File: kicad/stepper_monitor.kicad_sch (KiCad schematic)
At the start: 62 parts, among them J1 Conn_01x04_Pin, J2 Conn_01x04_Pin, J3 Conn_01x02_Pin, J4 USB_C_Receptacle_USB2.0, J5 JTAG, J6 Conn_01x04_Pin, M1 Motor-simple_stepper_motor_an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, Q1 MMDT2222A, SW1 SW_Push, U1 5V, U2 CP2102N-A01-GQFN28, U3 AMS1117-3.3, U4 CC6920BSO-5A, U5 CC6920BSO-5A, U6 ESP32-WROOM-32U-N4

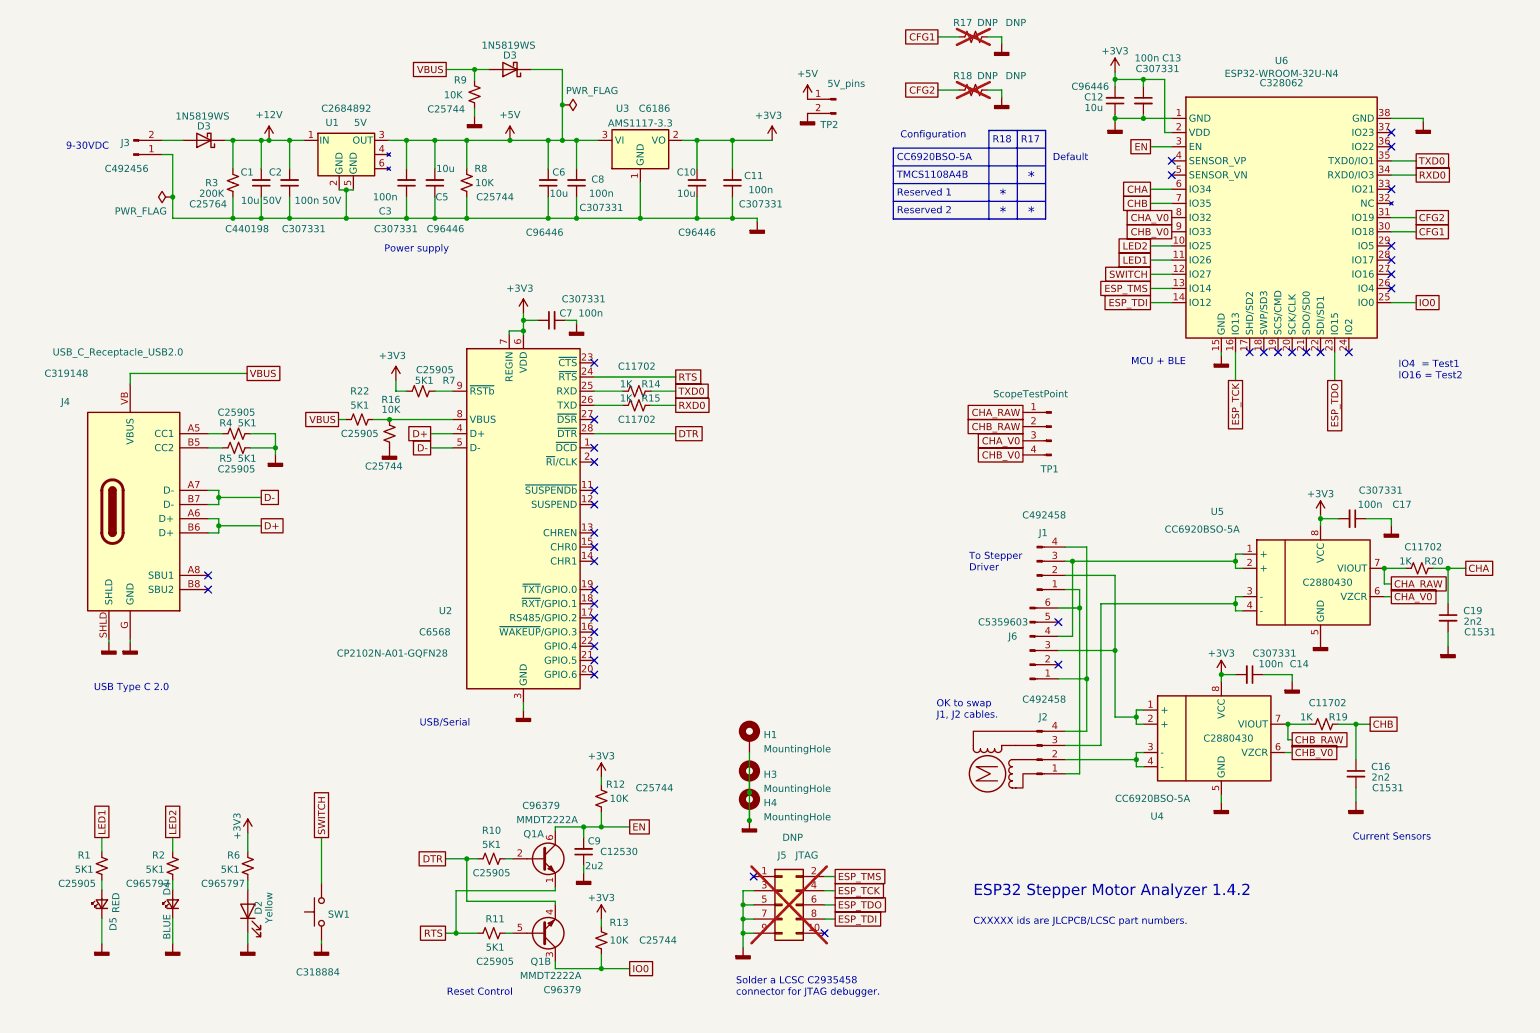
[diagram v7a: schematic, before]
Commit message: Routed opamp for voltage measurement. Added 4th mount hole
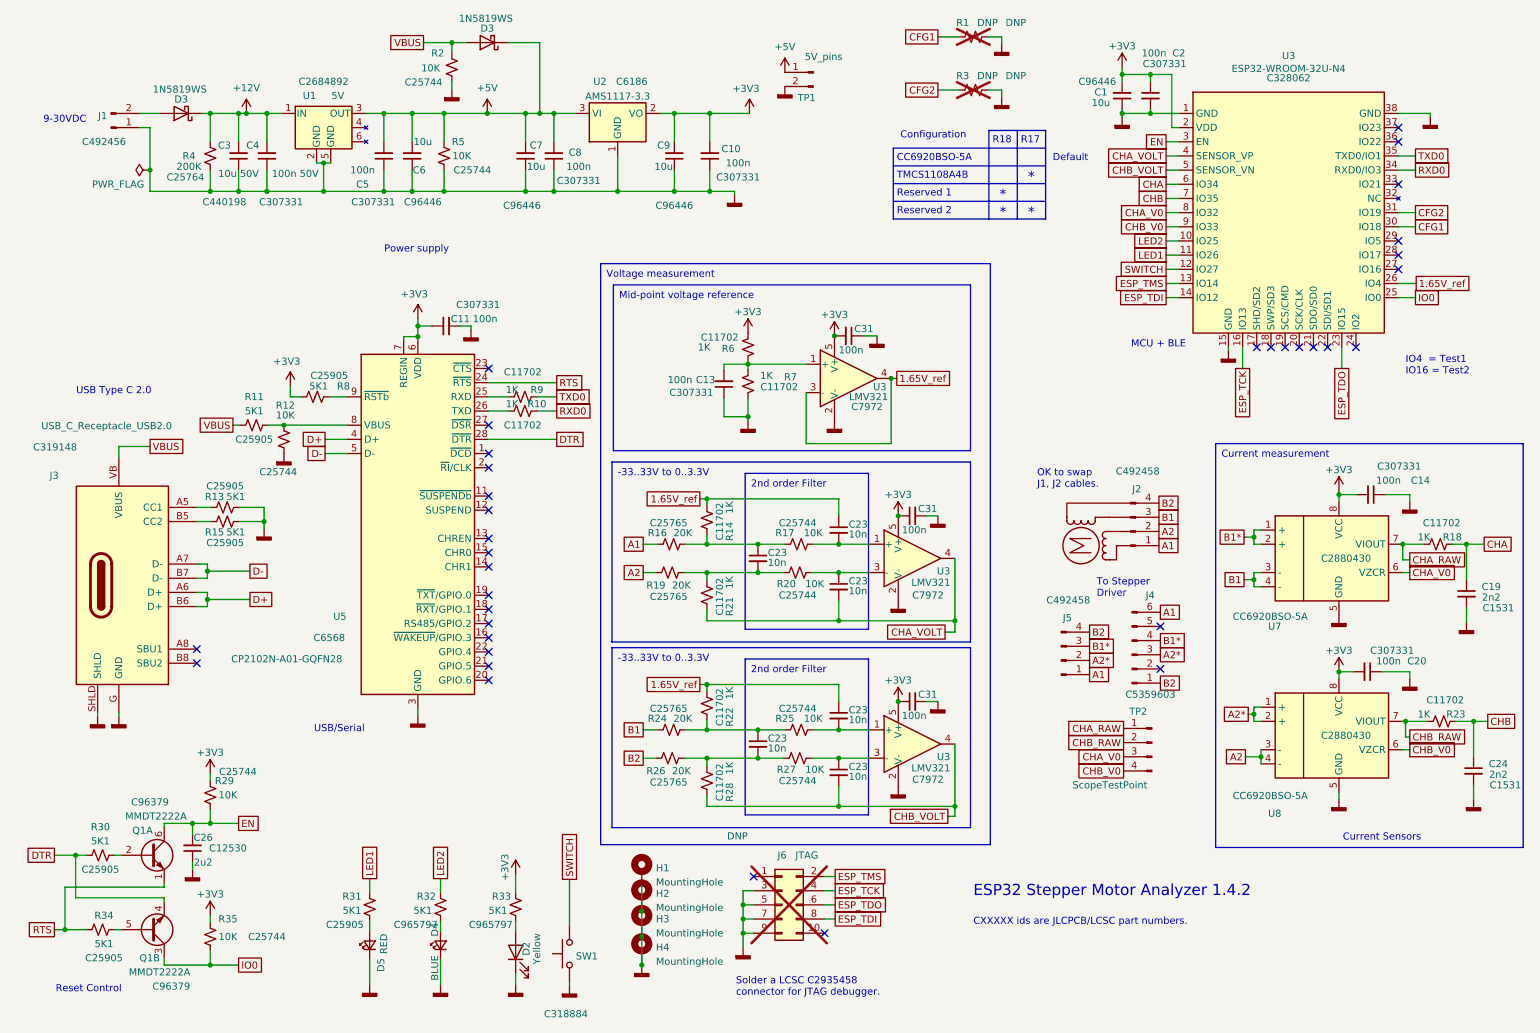
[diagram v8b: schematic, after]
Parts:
- added C13, C31 (x3): 100n, Capacitor_SMD:C_0402_1005Metric, symbol Device:C_Small
- added C23 (x6): 10n, Capacitor_SMD:C_0402_1005Metric, symbol Device:C_Small
- added H2: MountingHole, MountingHole:MountingHole_3.2mm_M3_Pad_Via, symbol Mechanical:MountingHole_Pad
- added R14, R21, R22, R28, R6, R7: 1K, Resistor_SMD:R_0402_1005Metric, symbol Device:R_Small_US
- added R16, R19, R24, R26: 20K, Resistor_SMD:R_0402_1005Metric, symbol Device:R_Small_US
- added R17, R20, R25, R27: 10K, Resistor_SMD:R_0402_1005Metric, symbol Device:R_Small_US
- added U3 (x3): LMV321, Package_TO_SOT_SMD:SOT-23-5, symbol Amplifier_Operational:LMV321
- renumbered C12 to C1, C11 to C10, C7 to C11, C17 to C14, C13 to C2, C14 to C20, C16 to C24, C9 to C26, C1 to C3, C2 to C4, C3 to C5, C5 to C6, C6 to C7, C10 to C9, J3 to J1, J4 to J3, J6 to J4, J1 to J5, J5 to J6, R17 to R1, R15 to R10, R22 to R11, R16 to R12, R4 to R13, R5 to R15, R20 to R18, R9 to R2, R19 to R23, R12 to R29, R18 to R3, R10 to R30, R1 to R31, R2 to R32, R6 to R33, R11 to R34, R13 to R35, R3 to R4, R8 to R5, R7 to R8, R14 to R9, TP2 to TP1, TP1 to TP2, U3 to U2, U6 to U3, U2 to U5, U5 to U7, U4 to U8
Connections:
- net +3V3: now also C31.1, C31.1, C31.2, R6.1, U3.5 (V+), U3.5 (V+), U3.5 (V+)
- net GNDD: now also C13.1, C31.1, C31.2, C31.2, H2.1, R7.2, U3.2 (V-), U3.2 (V-), U3.2 (V-)
- net 1.65V_ref: now reaches U3.26 (IO4)
- net 1.65V_ref: now also C23.1, C23.1, R14.2, R22.2, U3.3 (-), U3.4
- net CHA_VOLT: now reaches U3.4 (SENSOR_VP)
- net CHA_VOLT: now also C23.2, R21.1, U3.4
- net CHB_VOLT: now reaches U3.5 (SENSOR_VN)
- net CHB_VOLT: now also C23.2, R28.1, U3.4
- net A1: now reaches J2.1 (Pin_1), J4.6 (Pin_6), J5.1 (Pin_1)
- net A1: now also R16.2
- net A2: now reaches J2.2 (Pin_2), U8.3 (-), U8.4 (-)
- net A2: now also R19.2
- net B1: now reaches J2.3 (Pin_3), U7.3 (-), U7.4 (-)
- net B1: now also R24.2
- net B2: now reaches J2.4 (Pin_4), J4.1 (Pin_1), J5.4 (Pin_4)
- net B2: now also R26.2
- net A2*: now reaches J4.3 (Pin_3), J5.2 (Pin_2), U8.1 (+), U8.2 (+)
- net B1*: now reaches J4.4 (Pin_4), J5.3 (Pin_3), U7.1 (+), U7.2 (+)
- new net: C23.1, R27.1, U3.3 (-)
- new net: C23.1, R14.1, R16.1, R17.2
- new net: C23.2, R19.1, R20.2, R21.2
- new net: C13.2, R6.2, R7.1, U3.1 (+)
- new net: C23.2, R26.1, R27.2, R28.2
- new net: C23.2, R17.1, U3.1 (+)
- new net: C23.1, R20.1, U3.3 (-)
- new net: C23.1, R22.1, R24.1, R25.2
- new net: C23.2, R25.1, U3.1 (+)
- no-connect marks 38 -> 35
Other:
- moved on the sheet: C1, C10, C11, C14, C19, C2, C20, C24, C26, C3, C4, C5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
